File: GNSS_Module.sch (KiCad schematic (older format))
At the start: 12 parts

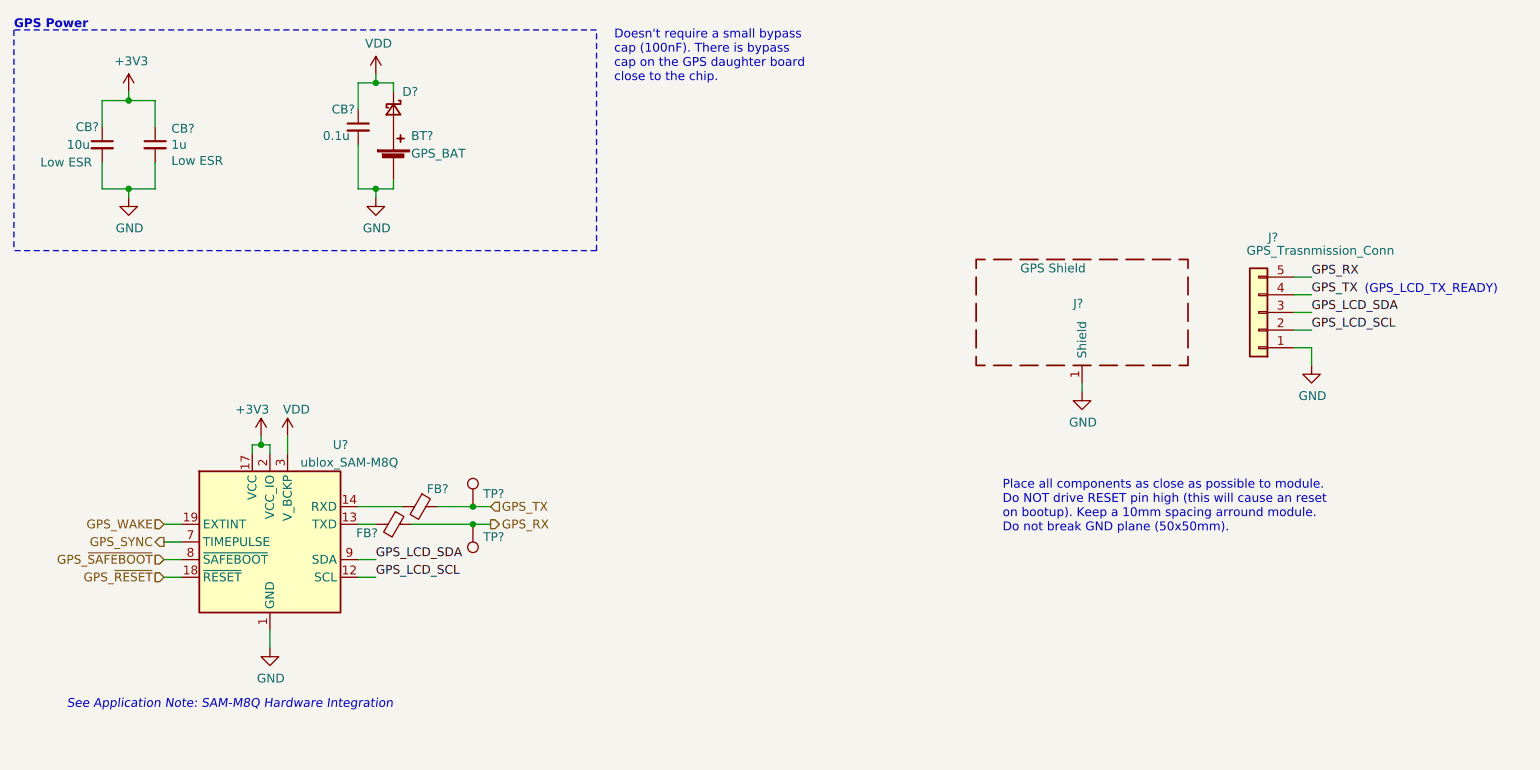
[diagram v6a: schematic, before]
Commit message: Add PWR Flags
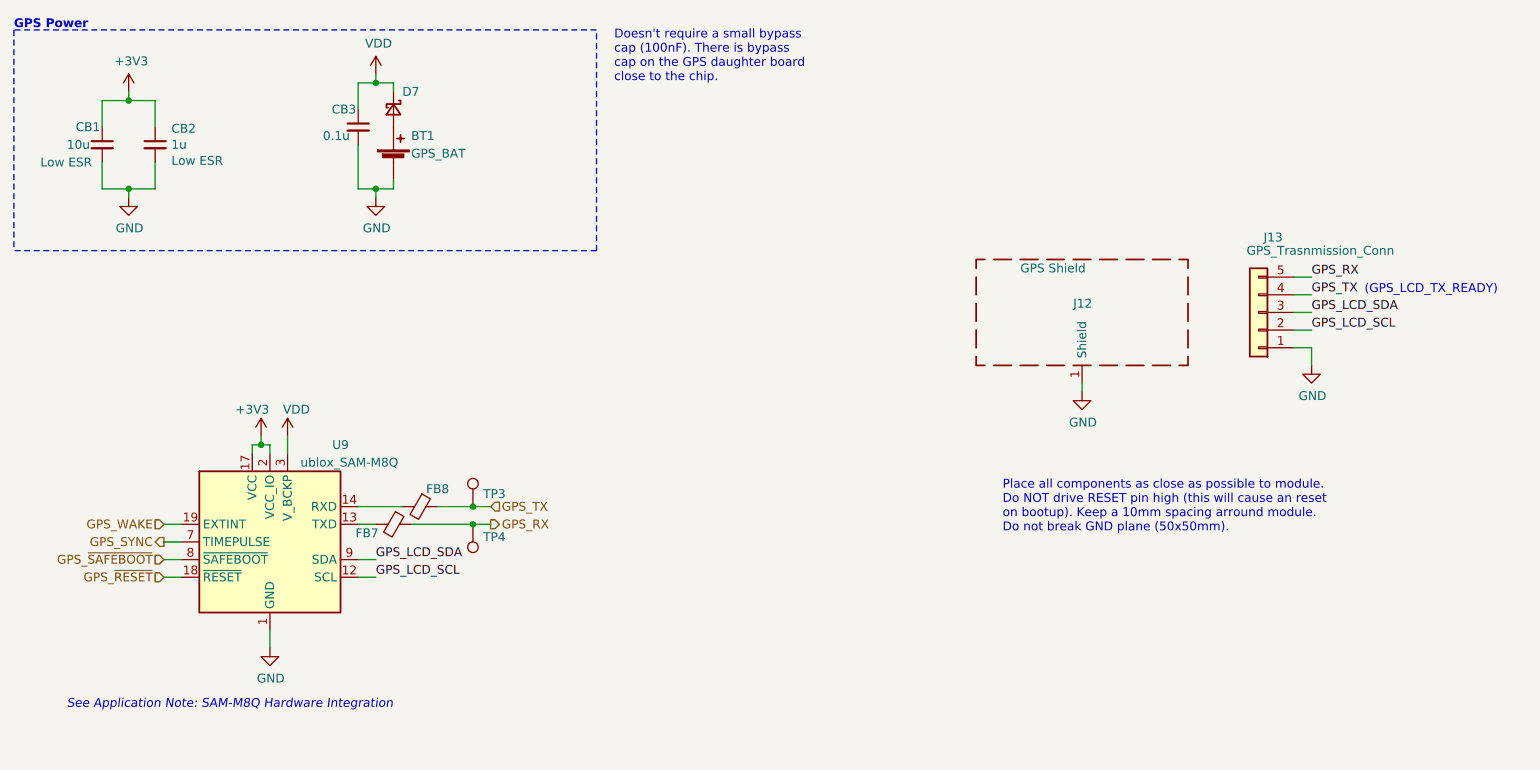
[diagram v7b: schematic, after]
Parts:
- gave numbers to parts that had none: 12
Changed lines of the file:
@@
 P 3050 3750
 AR Path="/5EE051F9" Ref="U?"  Part="1"
-AR Path="/5EDF3693/5EE051F9" Ref="U?"  Part="1"
-F 0 "U?" H 3450 4300 50  0000 C CNN
+AR Path="/5EDF3693/5EE051F9" Ref="U9"  Part="1"
+F 0 "U9" H 3450 4300 50  0000 C CNN
 F 1 "ublox_SAM-M8Q" H 3500 4200 50  0000 C CNN
 F 2 "RF_GPS:ublox_SAM-M8Q" H 3550 3300 50  0001 C CNN
@@
 P 2250 1800
 AR Path="/5EE05200" Ref="#PWR?"  Part="1"
-AR Path="/5EDF3693/5EE05200" Ref="#PWR?"  Part="1"
-F 0 "#PWR?" H 2250 1550 50  0001 C CNN
+AR Path="/5EDF3693/5EE05200" Ref="#PWR0100"  Part="1"
+F 0 "#PWR0100" H 2250 1550 50  0001 C CNN
 F 1 "GND" H 2255 1627 50  0000 C CNN
 F 2 "" H 2250 1800 50  0001 C CNN
@@
 P 2250 1200
 AR Path="/5EE05208" Ref="#PWR?"  Part="1"
-AR Path="/5EDF3693/5EE05208" Ref="#PWR?"  Part="1"
-F 0 "#PWR?" H 2250 1050 50  0001 C CNN
+AR Path="/5EDF3693/5EE05208" Ref="#PWR099"  Part="1"
+F 0 "#PWR099" H 2250 1050 50  0001 C CNN
 F 1 "+3V3" H 2265 1373 50  0000 C CNN
 F 2 "" H 2250 1200 50  0001 C CNN
@@
 P 3650 1800
 AR Path="/5EE0520E" Ref="#PWR?"  Part="1"
-AR Path="/5EDF3693/5EE0520E" Ref="#PWR?"  Part="1"
-F 0 "#PWR?" H 3650 1550 50  0001 C CNN
+AR Path="/5EDF3693/5EE0520E" Ref="#PWR0105"  Part="1"
+F 0 "#PWR0105" H 3650 1550 50  0001 C CNN
 F 1 "GND" H 3655 1627 50  0000 C CNN
 F 2 "" H 3650 1800 50  0001 C CNN
@@
 P 3000 3150
 AR Path="/5EE05214" Ref="#PWR?"  Part="1"
-AR Path="/5EDF3693/5EE05214" Ref="#PWR?"  Part="1"
-F 0 "#PWR?" H 3000 3000 50  0001 C CNN
+AR Path="/5EDF3693/5EE05214" Ref="#PWR0101"  Part="1"
+F 0 "#PWR0101" H 3000 3000 50  0001 C CNN
 F 1 "+3V3" H 2950 3300 50  0000 C CNN
 F 2 "" H 3000 3150 50  0001 C CNN
@@
 P 3050 4350
 AR Path="/5EE05234" Ref="#PWR?"  Part="1"
-AR Path="/5EDF3693/5EE05234" Ref="#PWR?"  Part="1"
-F 0 "#PWR?" H 3050 4100 50  0001 C CNN
+AR Path="/5EDF3693/5EE05234" Ref="#PWR0102"  Part="1"
+F 0 "#PWR0102" H 3050 4100 50  0001 C CNN
 F 1 "GND" H 3055 4177 50  0000 C CNN
 F 2 "" H 3050 4350 50  0001 C CNN
@@
 P 3750 3650
 AR Path="/5EE05241" Ref="FB?"  Part="1"
-AR Path="/5EDF3693/5EE05241" Ref="FB?"  Part="1"
-F 0 "FB?" V 3800 3500 50  0000 C CNN
+AR Path="/5EDF3693/5EE05241" Ref="FB7"  Part="1"
+F 0 "FB7" V 3800 3500 50  0000 C CNN
 F 1 "BLM15HD102SN1" V 3800 4000 50  0001 C CNN
 F 2 "" V 3680 3650 50  0001 C CNN
@@
 P 8650 2450
 AR Path="/5EE05249" Ref="J?"  Part="1"
-AR Path="/5EDF3693/5EE05249" Ref="J?"  Part="1"
-F 0 "J?" H 8568 2025 50  0000 C CNN
+AR Path="/5EDF3693/5EE05249" Ref="J13"  Part="1"
+F 0 "J13" H 8568 2025 50  0000 C CNN
 F 1 "GPS_Trasnmission_Conn" H 8300 2100 50  0000 C CNN
 F 2 "" H 8650 2450 50  0001 C CNN
@@
 P 8950 2750
 AR Path="/5EE0524F" Ref="#PWR?"  Part="1"
-AR Path="/5EDF3693/5EE0524F" Ref="#PWR?"  Part="1"
-F 0 "#PWR?" H 8950 2500 50  0001 C CNN
+AR Path="/5EDF3693/5EE0524F" Ref="#PWR0107"  Part="1"
+F 0 "#PWR0107" H 8950 2500 50  0001 C CNN
 F 1 "GND" H 8955 2577 50  0000 C CNN
 F 2 "" H 8950 2750 50  0001 C CNN
@@
 P 3750 1600
 AR Path="/5EE0526D" Ref="BT?"  Part="1"
-AR Path="/5EDF3693/5EE0526D" Ref="BT?"  Part="1"
-F 0 "BT?" H 3850 1750 50  0000 L CNN
+AR Path="/5EDF3693/5EE0526D" Ref="BT1"  Part="1"
+F 0 "BT1" H 3850 1750 50  0000 L CNN
 F 1 "GPS_BAT" H 3850 1650 50  0000 L CNN
 F 2 "" V 3750 1660 50  0001 C CNN
@@
 P 3750 1300
 AR Path="/5EE05273" Ref="D?"  Part="1"
-AR Path="/5EDF3693/5EE05273" Ref="D?"  Part="1"
-F 0 "D?" V 3650 1350 50  0000 L CNN
+AR Path="/5EDF3693/5EE05273" Ref="D7"  Part="1"
+F 0 "D7" V 3650 1350 50  0000 L CNN
 F 1 "~" V 3750 600 50  0000 L CNN
 F 2 "" V 3750 1300 50  0001 C CNN
@@
 P 2400 1500
 AR Path="/5EE0527F" Ref="CB?"  Part="1"
-AR Path="/5EDF3693/5EE0527F" Ref="CB?"  Part="1"
-F 0 "CB?" H 2492 1591 50  0000 L CNN
+AR Path="/5EDF3693/5EE0527F" Ref="CB2"  Part="1"
+F 0 "CB2" H 2492 1591 50  0000 L CNN
 F 1 "1u" H 2492 1500 50  0000 L CNN
 F 2 "" H 2400 1500 50  0001 C CNN
@@
 P 3550 1400
 AR Path="/5EE05285" Ref="CB?"  Part="1"
-AR Path="/5EDF3693/5EE05285" Ref="CB?"  Part="1"
-F 0 "CB?" H 3400 1500 50  0000 L CNN
+AR Path="/5EDF3693/5EE05285" Ref="CB3"  Part="1"
+F 0 "CB3" H 3400 1500 50  0000 L CNN
 F 1 "0.1u" H 3350 1350 50  0000 L CNN
 F 2 "" H 3550 1400 50  0001 C CNN
@@
 P 2100 1500
 AR Path="/5EE0528E" Ref="CB?"  Part="1"
-AR Path="/5EDF3693/5EE0528E" Ref="CB?"  Part="1"
-F 0 "CB?" H 1950 1600 50  0000 L CNN
+AR Path="/5EDF3693/5EE0528E" Ref="CB1"  Part="1"
+F 0 "CB1" H 1950 1600 50  0000 L CNN
 F 1 "10u" H 1900 1500 50  0000 L CNN
 F 2 "" H 2100 1500 50  0001 C CNN
@@
 P 7650 2900
 AR Path="/5EE052A0" Ref="#PWR?"  Part="1"
-AR Path="/5EDF3693/5EE052A0" Ref="#PWR?"  Part="1"
-F 0 "#PWR?" H 7650 2650 50  0001 C CNN
+AR Path="/5EDF3693/5EE052A0" Ref="#PWR0106"  Part="1"
+F 0 "#PWR0106" H 7650 2650 50  0001 C CNN
 F 1 "GND" H 7655 2727 50  0000 C CNN
 F 2 "" H 7650 2900 50  0001 C CNN
@@
 P 3650 1100
 AR Path="/5EE052A8" Ref="#PWR?"  Part="1"
-AR Path="/5EDF3693/5EE052A8" Ref="#PWR?"  Part="1"
-F 0 "#PWR?" H 3650 950 50  0001 C CNN
+AR Path="/5EDF3693/5EE052A8" Ref="#PWR0104"  Part="1"
+F 0 "#PWR0104" H 3650 950 50  0001 C CNN
 F 1 "VDD" H 3665 1273 50  0000 C CNN
 F 2 "" H 3650 1100 50  0001 C CNN
@@
 P 3150 3150
 AR Path="/5EE052B2" Ref="#PWR?"  Part="1"
-AR Path="/5EDF3693/5EE052B2" Ref="#PWR?"  Part="1"
-F 0 "#PWR?" H 3150 3000 50  0001 C CNN
+AR Path="/5EDF3693/5EE052B2" Ref="#PWR0103"  Part="1"
+F 0 "#PWR0103" H 3150 3000 50  0001 C CNN
 F 1 "VDD" H 3200 3300 50  0000 C CNN
 F 2 "" H 3150 3150 50  0001 C CNN
@@
 P 3900 3550
 AR Path="/5EE19301" Ref="FB?"  Part="1"
-AR Path="/5EDF3693/5EE19301" Ref="FB?"  Part="1"
-F 0 "FB?" V 3800 3650 50  0000 C CNN
+AR Path="/5EDF3693/5EE19301" Ref="FB8"  Part="1"
+F 0 "FB8" V 3800 3650 50  0000 C CNN
 F 1 "BLM15HD102SN1" V 3950 3900 50  0001 C CNN
 F 2 "" V 3830 3550 50  0001 C CNN
@@
 P 7650 2450
 AR Path="/5EE0529A" Ref="J?"  Part="1"
-AR Path="/5EDF3693/5EE0529A" Ref="J?"  Part="1"
-F 0 "J?" H 7600 2500 50  0000 L CNN
+AR Path="/5EDF3693/5EE0529A" Ref="J12"  Part="1"
+F 0 "J12" H 7600 2500 50  0000 L CNN
 F 1 "GPS Shield" H 7300 2700 50  0000 L CNN
 F 2 "" H 7650 2350 50  0001 C CNN
@@
 Doesn't require a small bypass \ncap (100nF). There is bypass \ncap on the GPS daughter board \nclose to the chip.
 $Comp
-L Connector:TestPoint TP?
+L Connector:TestPoint TP4
 U 1 1 5F029AD8
 P 4200 3650
-F 0 "TP?" H 4142 3722 50  0000 R CNN
+F 0 "TP4" H 4142 3722 50  0000 R CNN
 F 1 "TestPoint" H 4258 3677 50  0001 L CNN
 F 2 "" H 4400 3650 50  0001 C CNN
@@
 	4200 3650 4300 3650
 $Comp
-L Connector:TestPoint TP?
+L Connector:TestPoint TP3
 U 1 1 5F029627
 P 4200 3550
-F 0 "TP?" H 4258 3622 50  0000 L CNN
+F 0 "TP3" H 4258 3622 50  0000 L CNN
 F 1 "TestPoint" H 4258 3577 50  0001 L CNN
 F 2 "" H 4400 3550 50  0001 C CNN
